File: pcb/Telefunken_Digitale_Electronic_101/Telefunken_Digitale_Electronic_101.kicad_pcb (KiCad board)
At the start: 2 copper layers, 100 x 52 mm, 40 parts, among them J1 Conn_01x02_Socket, J10 Conn_01x03_Socket, J2 Conn_01x02_Socket, J3 Conn_01x02_Socket, J4 Conn_01x02_Socket, J5 Conn_01x02_Socket, J6 Conn_01x02_Socket, J7 Conn_01x02_Socket, J8 Conn_01x04_Socket, J9 Conn_01x04_Socket, SW1 SW_Push, SW2 SW_Push, U1 TM1637_SOP20, U3 DS3231

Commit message: PCB: initial layout idea
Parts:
- moved R1 35.6 mm to (165.0, 73.0)
- moved C1 32.0 mm to (161.5, 70.9)
- moved C2 32.0 mm to (163.2, 72.0)
- moved R2 32.0 mm to (163.2, 75.5)
- moved C4 27.2 mm to (165.2, 77.2), turned to -90 degrees
- moved C3 25.5 mm to (161.5, 77.0), turned to -90 degrees
- moved U1 15.3 mm to (154.2, 75.5), turned to 0 degrees
- moved J8 2.51 mm to (161.1, 94.5)
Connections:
- J10 pad 2: /Buttons/SLOW -> /Buttons/TIME
- J10 pad 3: /Buttons/FAST -> /Buttons/SIGNAL
- J8 pad 1: /Interface/RTC_SCL -> /Interface/RTC_SDA
- J8 pad 2: /Interface/RTC_SDA -> /Interface/RTC_SCL
- J9 pad 1: /Buttons/ILLUM -> /Buttons/SLEEP_FRONT
- J9 pad 2: /Buttons/SLEEP_FRONT -> /Buttons/ILLUM
- J9 pad 3: /Buttons/SIGNAL -> /Buttons/FAST
- J9 pad 4: /Buttons/TIME -> /Buttons/SLOW
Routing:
- net VCC: track 0.00 -> 93.7 mm
- net /Interface/RTC_SDA: track 0.00 -> 44.8 mm
- net /Interface/RTC_SCL: track 0.00 -> 44.3 mm
- net /Buttons/SLEEP_TOP: track 0.00 -> 42.8 mm
- net /Buttons/FAST: track 0.00 -> 41.2 mm
- net /Interface/RTC_SQW: track 0.00 -> 39.5 mm
- net /Interface/RTC_32K: track 0.00 -> 39.0 mm
- net /Buttons/TIME: track 0.00 -> 35.6 mm
- net /Display/CLK: track 0.00 -> 35.3 mm, vias 0 -> 2
- net /Display/DIO: track 0.00 -> 33.5 mm, vias 0 -> 2
- net GND: track 0.00 -> 30.5 mm
- net /Buttons/SIGNAL: track 0.00 -> 28.1 mm
- net Net-(DISPLAY1-CA4): track 0.00 -> 26.5 mm
- net /Buttons/SLEEP_FRONT: track 0.00 -> 21.3 mm
- net Net-(DISPLAY1-c): track 0.00 -> 20.6 mm
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
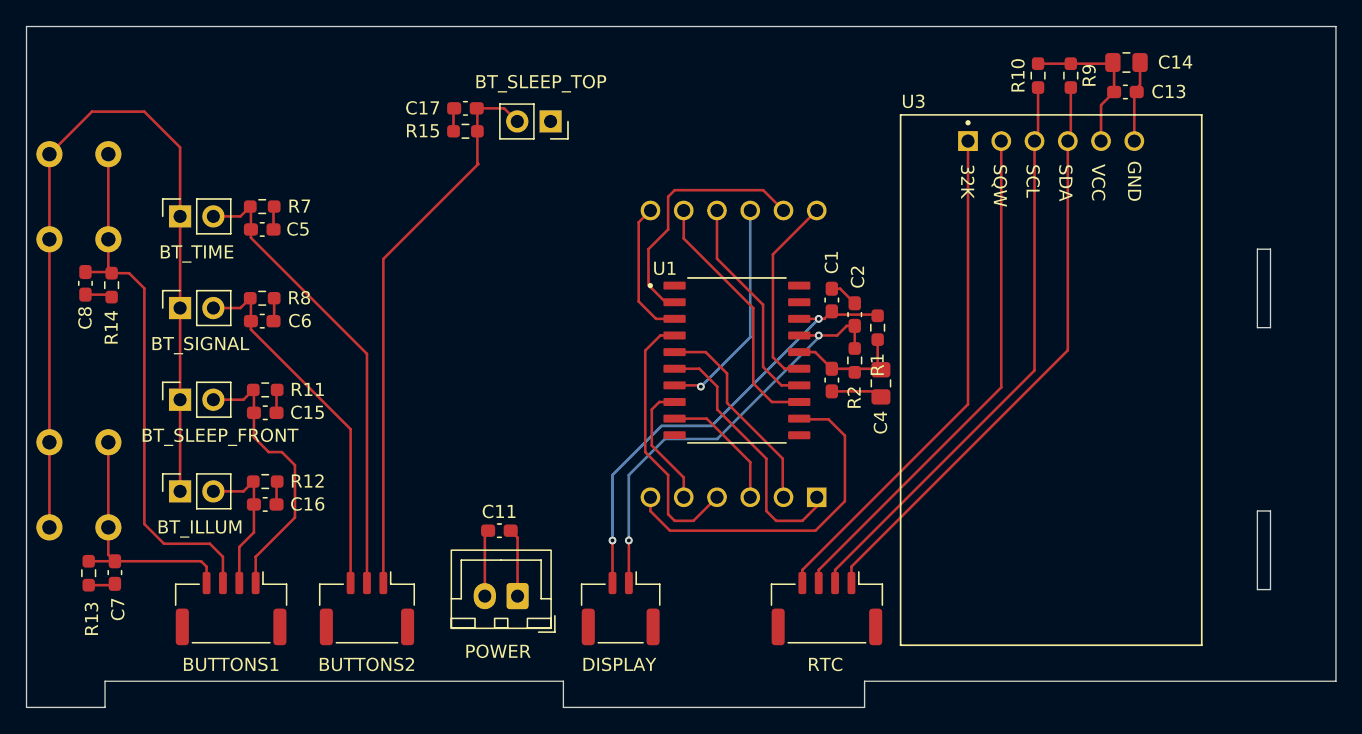
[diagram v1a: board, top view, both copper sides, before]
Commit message: PCB: updated with new button reading strategy (still missing VCC and GND routing)
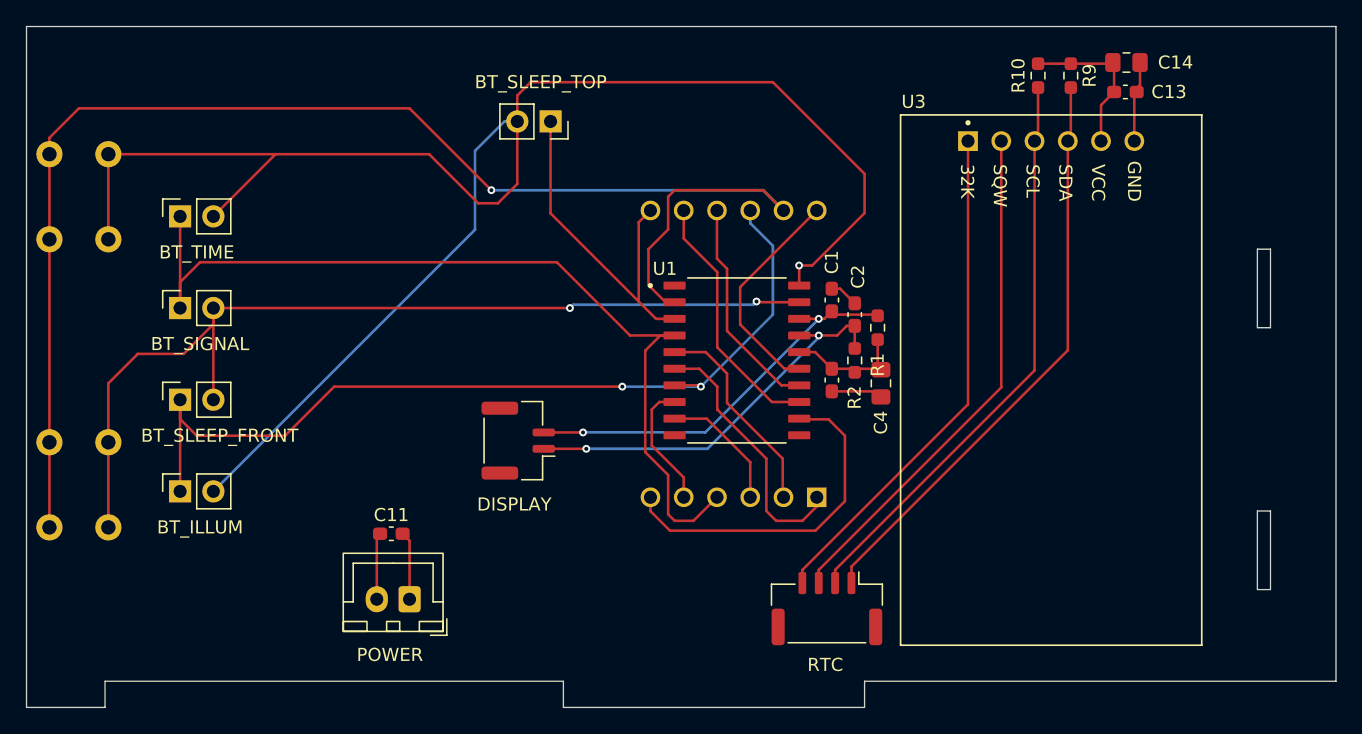
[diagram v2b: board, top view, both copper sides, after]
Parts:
- removed C15, C16, C17, C5, C6, C7, C8: 100n, Capacitor_SMD:C_0603_1608Metric_Pad1.08x0.95mm_HandSolder
- removed J10: Conn_01x03_Socket, Connector_JST:JST_GH_BM03B-GHS-TBT_1x03-1MP_P1.25mm_Vertical
- removed J9: Conn_01x04_Socket, Connector_JST:JST_GH_BM04B-GHS-TBT_1x04-1MP_P1.25mm_Vertical
- removed R11, R12, R13, R14, R15, R7, R8: 10k, Resistor_SMD:R_0603_1608Metric_Pad0.98x0.95mm_HandSolder
- moved J7 15.0 mm to (137.6, 81.6), turned to 90 degrees
- moved C11 8.25 mm to (127.9, 88.7)
- moved J6 8.25 mm to (129.2, 93.7)
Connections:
- DISPLAY1 pad 10: Net-(DISPLAY1-f) -> /Buttons/GRID4
- DISPLAY1 pad 11: Net-(DISPLAY1-a) -> /Buttons/GRID1
- DISPLAY1 pad 4: Net-(DISPLAY1-c) -> /Buttons/GRID3
- DISPLAY1 pad 7: Net-(DISPLAY1-b) -> /Buttons/GRID2
- J1 pad 1: VCC -> /Buttons/GRID3
- J1 pad 2: /Buttons/TIME -> /Buttons/K2
- J2 pad 1: VCC -> /Buttons/GRID3
- J2 pad 2: /Buttons/SIGNAL -> /Buttons/K1
- J3 pad 1: VCC -> /Buttons/GRID4
- J3 pad 2: /Buttons/SLEEP_FRONT -> /Buttons/K1
- J4 pad 1: VCC -> /Buttons/GRID4
- J4 pad 2: /Buttons/ILLUM -> /Buttons/K2
- J5 pad 1: VCC -> /Buttons/GRID2
- J5 pad 2: /Buttons/SLEEP_TOP -> /Buttons/K2
- SW1 pad 1: VCC -> /Buttons/GRID1
- SW1 pad 2: /Buttons/FAST -> /Buttons/K2
- SW2 pad 1: VCC -> /Buttons/GRID1
- SW2 pad 2: /Buttons/SLOW -> /Buttons/K1
- U1 pad 19: unconnected-(U1-K1-Pad19) -> /Buttons/K1
- U1 pad 2: Net-(DISPLAY1-a) -> /Buttons/GRID1
- U1 pad 20: unconnected-(U1-K2-Pad20) -> /Buttons/K2
- U1 pad 3: Net-(DISPLAY1-b) -> /Buttons/GRID2
- U1 pad 4: Net-(DISPLAY1-c) -> /Buttons/GRID3
- U1 pad 7: Net-(DISPLAY1-f) -> /Buttons/GRID4
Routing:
- net /Buttons/K2: track 0.00 -> 132.8 mm, vias 0 -> 1
- net /Buttons/GRID1: track 0.00 -> 109.5 mm, vias 0 -> 1
- net /Buttons/K1: track 0.00 -> 74.0 mm, vias 0 -> 2
- net /Buttons/GRID3: track 0.00 -> 70.3 mm
- net /Buttons/GRID4: track 0.00 -> 68.8 mm, vias 0 -> 2
- net VCC: track 93.7 -> 26.5 mm
- net /Buttons/SLEEP_TOP: track 42.8 -> 0.00 mm
- net /Buttons/FAST: track 41.2 -> 0.00 mm
- net /Buttons/TIME: track 35.6 -> 0.00 mm
- net /Buttons/SIGNAL: track 28.1 -> 0.00 mm
- net /Buttons/GRID2: track 0.00 -> 27.1 mm
- net /Buttons/SLEEP_FRONT: track 21.3 -> 0.00 mm
- net Net-(DISPLAY1-c): track 20.6 -> 0.00 mm
- net /Buttons/SLOW: track 19.7 -> 0.00 mm
- net Net-(DISPLAY1-a): track 19.6 -> 0.00 mm
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
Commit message: PCB: refined layout, added GND planes, connected VCC
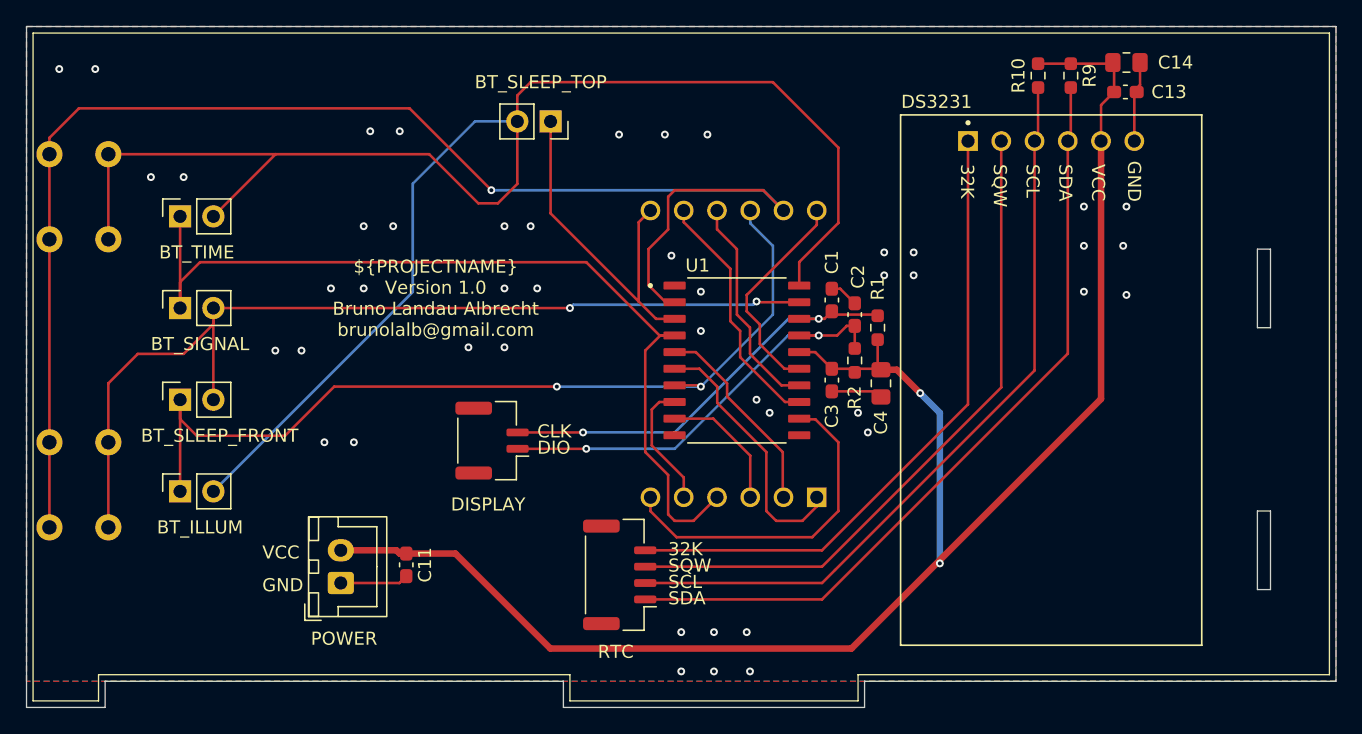
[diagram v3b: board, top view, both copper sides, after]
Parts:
- moved J8 16.0 mm to (145.3, 91.9), turned to 90 degrees
- moved J6 5.39 mm to (124.0, 92.5), turned to 90 degrees
- moved C11 2.63 mm to (129.0, 91.1), turned to -90 degrees
- moved J7 2.00 mm to (135.6, 81.6)
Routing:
- net VCC: track 26.5 -> 127.5 mm, vias 0 -> 2
- net /Interface/RTC_SDA: track 44.8 -> 60.5 mm
- net /Interface/RTC_SCL: track 44.3 -> 58.2 mm
- net /Interface/RTC_SQW: track 39.5 -> 51.7 mm
- net /Interface/RTC_32K: track 39.0 -> 49.4 mm
- net /Display/CLK: track 31.0 -> 33.0 mm
- net /Display/DIO: track 30.9 -> 32.9 mm
- net /Buttons/K2: track 132.8 -> 131.9 mm, vias 1 -> 0
- net Net-(DISPLAY1-CA3): track 19.5 -> 18.9 mm
- net GND: vias 0 -> 46
- added copper zone on B.Cu, net GND
- added copper zone on F.Cu, net GND
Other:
- board text added: "${PROJECTNAME} Version ${REVISION} ${COMMENT1} ${COMPANY}"
- board text added: "32K"
- board text added: "CLK"
- board text added: "DIO"
- board text added: "GND"
- board text added: "SCL"
- board text added: "SDA"
- board text added: "SQW"
- board text added: "VCC"

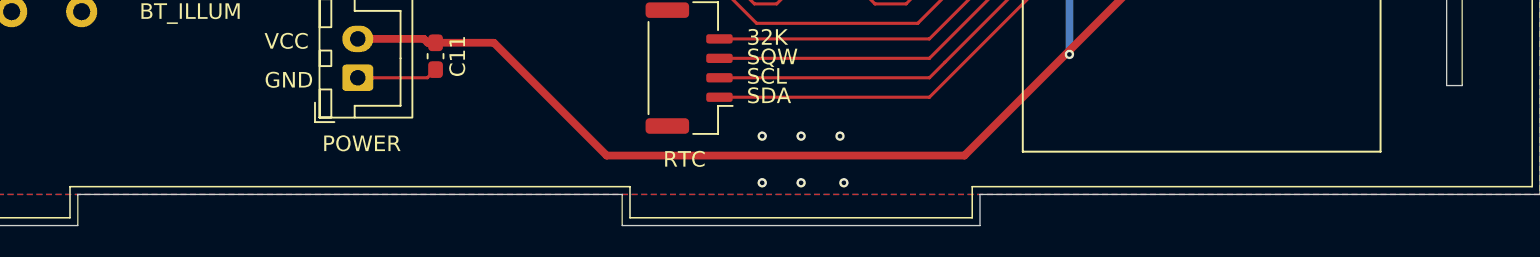
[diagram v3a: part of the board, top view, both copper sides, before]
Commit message: SCH and PCB: added the Mounting Pads (a few chosen ones)
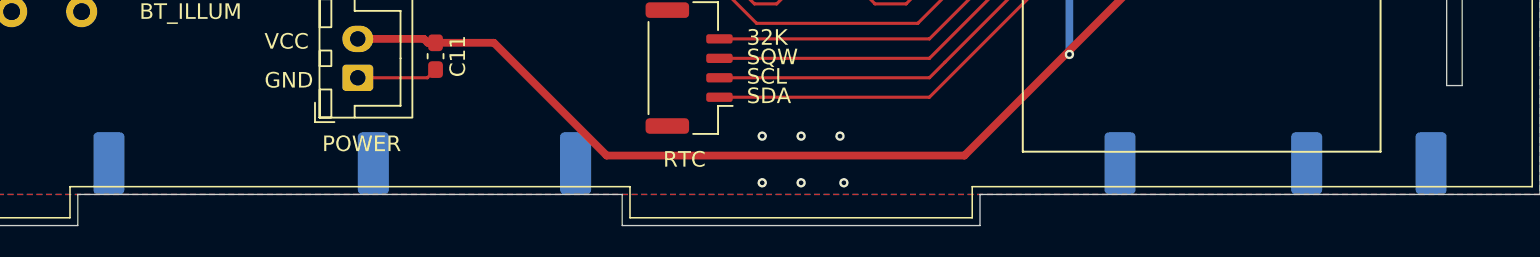
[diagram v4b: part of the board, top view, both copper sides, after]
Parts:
- added H1: MountingHole_Pad_MP, RadioWecker:BOARD_TO_BOARD_PAD_SMD, B.Cu at (109.0, 100.0)
- added H2: MountingHole_Pad_MP, RadioWecker:BOARD_TO_BOARD_PAD_SMD, B.Cu at (126.0, 100.0)
- added H3: MountingHole_Pad_MP, RadioWecker:BOARD_TO_BOARD_PAD_SMD, B.Cu at (139.0, 100.0)
- added H4: MountingHole_Pad_MP, RadioWecker:BOARD_TO_BOARD_PAD_SMD, B.Cu at (174.0, 100.0)
- added H5: MountingHole_Pad_MP, RadioWecker:BOARD_TO_BOARD_PAD_SMD, B.Cu at (186.0, 100.0)
- added H6: MountingHole_Pad_MP, RadioWecker:BOARD_TO_BOARD_PAD_SMD, B.Cu at (194.0, 100.0)

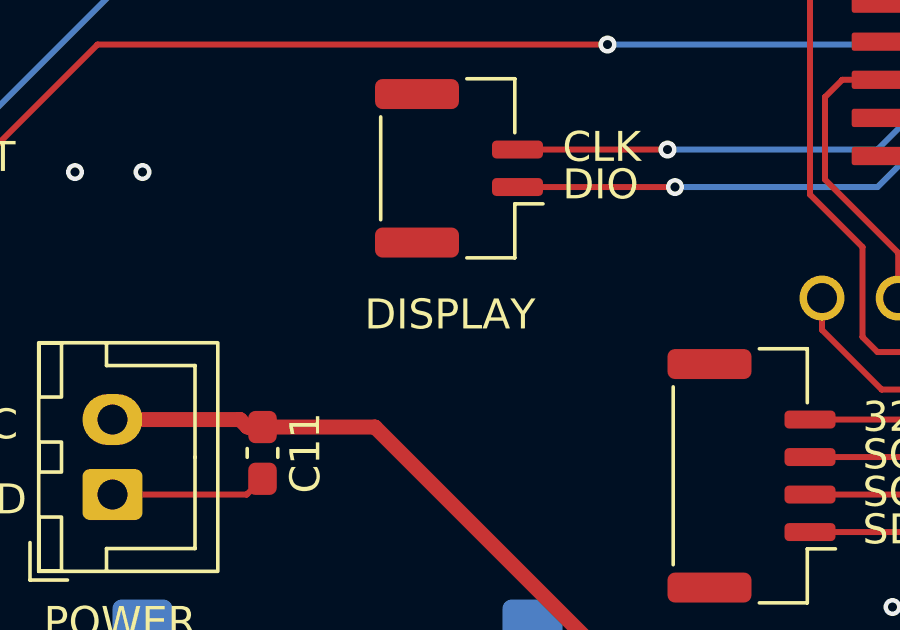
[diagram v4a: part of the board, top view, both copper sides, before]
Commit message: SCH - interface: replaced symbols from connectors with mounting pads to contain the mounting pads (and connected them to GND)
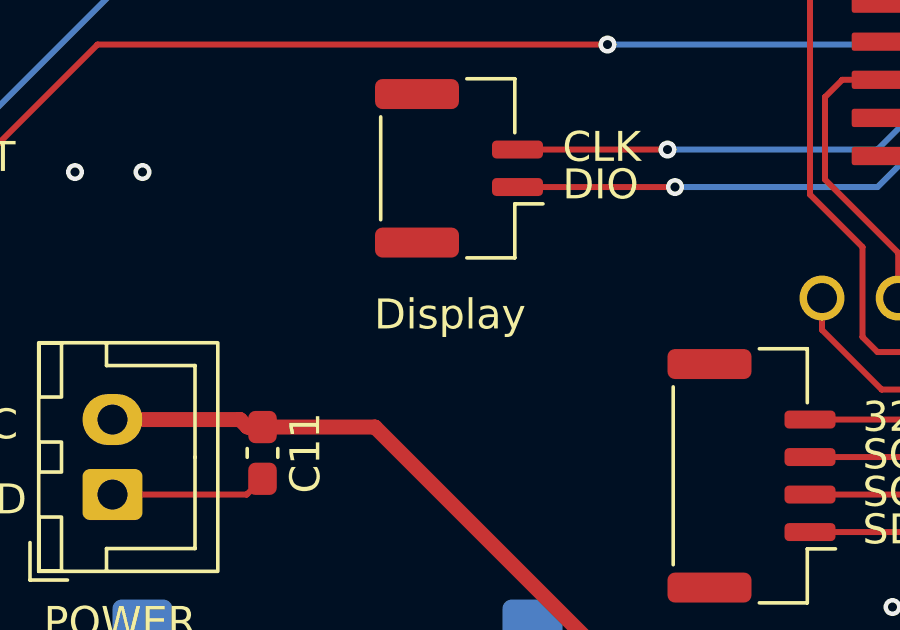
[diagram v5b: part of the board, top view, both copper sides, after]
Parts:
- J7: value Conn_01x02_Socket -> Conn_01x02_MountingPin
- J8: value Conn_01x04_Socket -> Conn_01x04_MountingPin
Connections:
- J7 pad MP: (no net) -> GND
- J8 pad MP: (no net) -> GND
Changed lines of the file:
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@@
 			)
 		)
-		(property "Value" "Conn_01x02_Socket"
+		(property "Value" "Conn_01x02_MountingPin"
 			(at 0 4 90)
 			(layer "F.Fab")
@@
 			)
 		)
-		(property "Description" "Generic connector, single row, 01x02, script generated"
+		(property "Description" "Generic connectable mounting pin connector, single row, 01x02, script generated (kicad-library-utils/schlib/autogen/connector/)"
 			(at 0 0 90)
 			(layer "F.Fab")
@@
 			)
 		)
-		(property "Name" "DISPLAY"
+		(property "Name" "Display"
 			(at -4.875 -0.3 0)
 			(unlocked yes)
@@
 			)
 		)
-		(property ki_fp_filters "Connector*:*_1x??_*")
+		(property ki_fp_filters "Connector*:*_1x??-1MP*")
 		(sheetname "/Interface/")
 		(sheetfile "interface.kicad_sch")
@@
 			(unit
 				(name "A")
-				(pins "1" "2")
+				(pins "1" "2" "MP")
 			)
 		)
@@
 			(layers "F.Cu" "F.Mask" "F.Paste")
 			(roundrect_rratio 0.25)
+			(net "GND")
+			(pinfunction "MountPin_MP")
+			(pintype "passive")
 		)
 		(pad "MP" smd roundrect
@@
 			(layers "F.Cu" "F.Mask" "F.Paste")
 			(roundrect_rratio 0.25)
+			(net "GND")
+			(pinfunction "MountPin_MP")
+			(pintype "passive")
 		)
 		(embedded_fonts no)
@@
 			)
 		)
-		(property "Value" "Conn_01x04_Socket"
+		(property "Value" "Conn_01x04_MountingPin"
 			(at 0 4 90)
 			(layer "F.Fab")
@@
 			)
 		)
-		(property "Description" "Generic connector, single row, 01x04, script generated"
+		(property "Description" "Generic connectable mounting pin connector, single row, 01x04, script generated (kicad-library-utils/schlib/autogen/connector/)"
 			(at 0 0 90)
 			(layer "F.Fab")
@@
 			)
 		)
-		(property ki_fp_filters "Connector*:*_1x??_*")
+		(property ki_fp_filters "Connector*:*_1x??-1MP*")
 		(sheetname "/Interface/")
 		(sheetfile "interface.kicad_sch")
@@
 			(unit
 				(name "A")
-				(pins "1" "2" "3" "4")
+				(pins "1" "2" "3" "4" "MP")
 			)
 		)
@@
 			(layers "F.Cu" "F.Mask" "F.Paste")
 			(roundrect_rratio 0.25)
+			(net "GND")
+			(pinfunction "MountPin_MP")
+			(pintype "passive")
 		)
 		(pad "MP" smd roundrect
@@
 			(layers "F.Cu" "F.Mask" "F.Paste")
 			(roundrect_rratio 0.25)
+			(net "GND")
+			(pinfunction "MountPin_MP")
+			(pintype "passive")
 		)
 		(embedded_fonts no)
